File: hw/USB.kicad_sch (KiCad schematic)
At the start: 4 parts, among them J3 USB_C_Receptacle_USB2.0, U3 PUSB3FR4

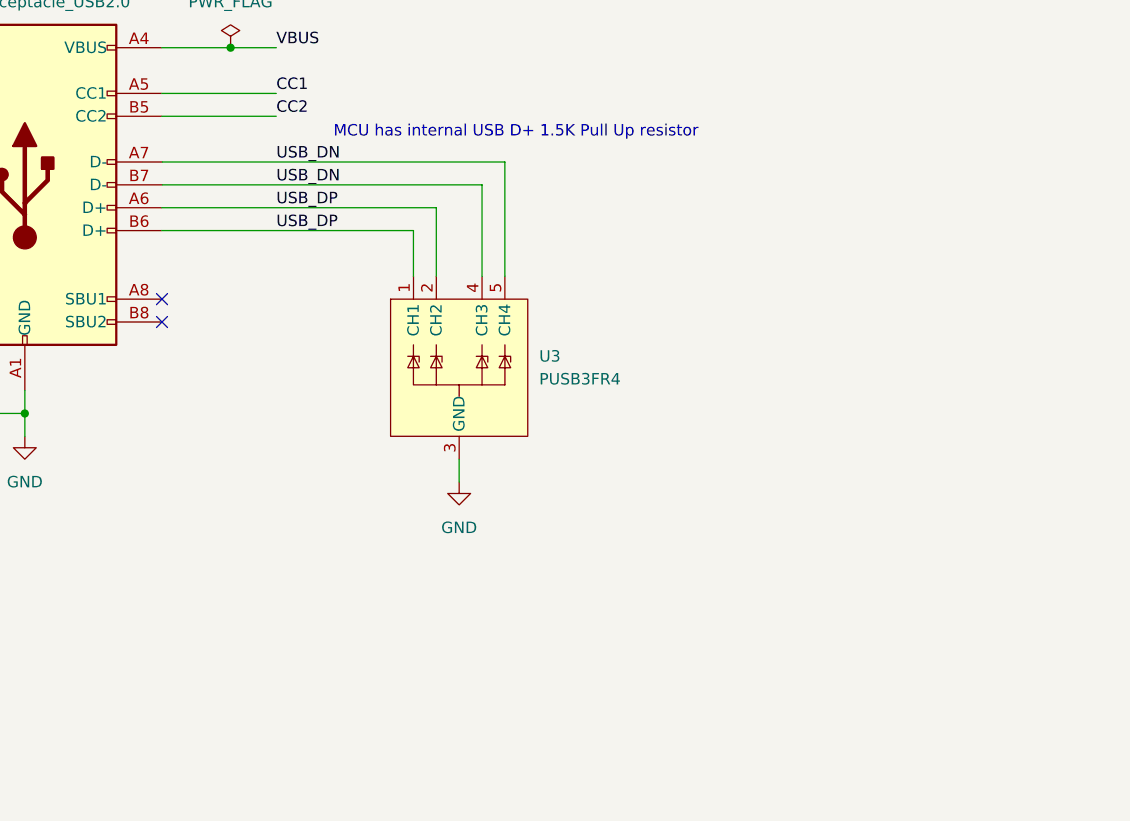
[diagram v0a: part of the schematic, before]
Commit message: routed USB
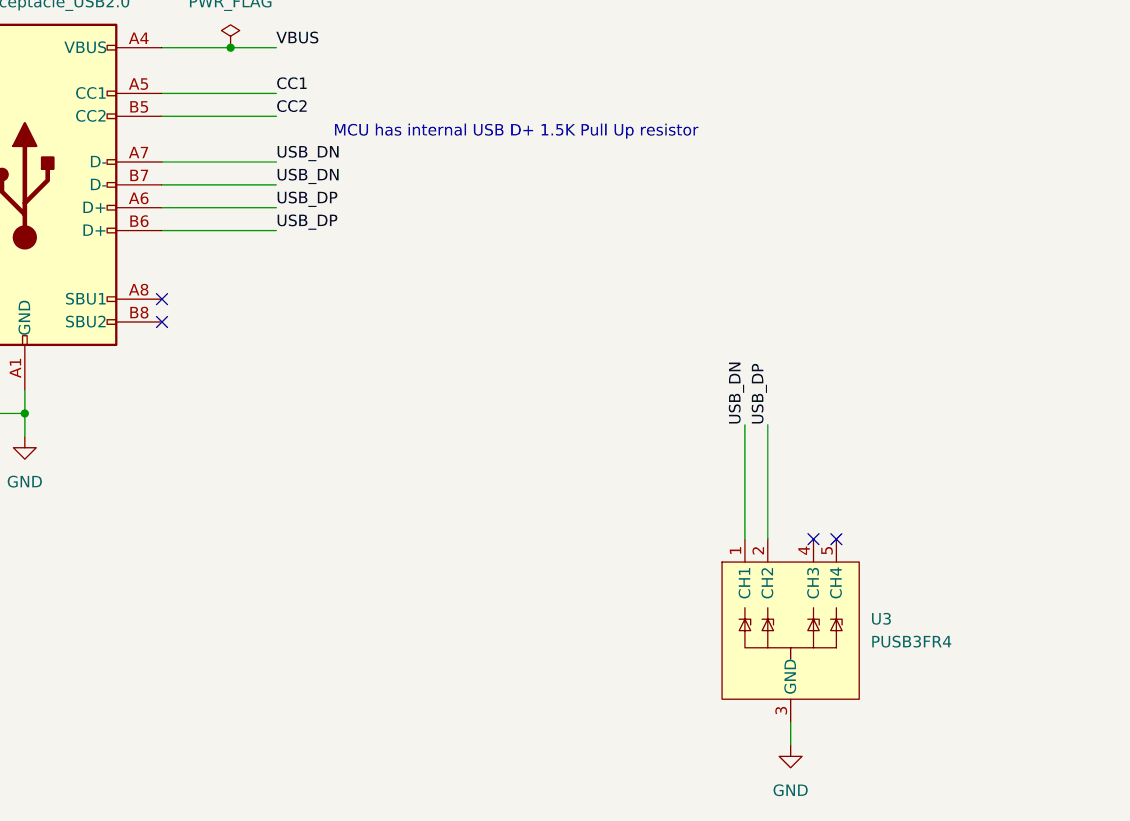
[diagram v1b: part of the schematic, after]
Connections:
- net USB_DN: now also U3.1 (CH1); no longer U3.4 (CH3), U3.5 (CH4)
- net USB_DP: no longer U3.1 (CH1)
- no-connect marks 2 -> 4
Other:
- moved on the sheet: U3
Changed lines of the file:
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@@
   (junction (at 48.26 106.68) (diameter 0) (color 0 0 0 0)
   )
+  (no_connect (at 138.43 120.65))
   (no_connect (at 63.5 93.98))
+  (no_connect (at 135.89 120.65))
   (no_connect (at 63.5 96.52))
   (wire (pts (xy 193.04 73.66) (xy 180.34 73.66))
@@
     (stroke (width 0) (type default))
   )
-  (wire (pts (xy 63.5 83.82) (xy 93.98 83.82))
+  (wire (pts (xy 63.5 83.82) (xy 76.2 83.82))
     (stroke (width 0) (type default))
   )
@@
     (stroke (width 0) (type default))
   )
-  (wire (pts (xy 63.5 81.28) (xy 99.06 81.28))
-    (stroke (width 0) (type default))
-  )
-  (wire (pts (xy 63.5 78.74) (xy 101.6 78.74))
-    (stroke (width 0) (type default))
-  )
-  (wire (pts (xy 101.6 91.44) (xy 101.6 78.74))
+  (wire (pts (xy 63.5 81.28) (xy 76.2 81.28))
+    (stroke (width 0) (type default))
+  )
+  (wire (pts (xy 63.5 78.74) (xy 76.2 78.74))
     (stroke (width 0) (type default))
   )
@@
     (stroke (width 0) (type default))
   )
-  (wire (pts (xy 91.44 91.44) (xy 91.44 86.36))
-    (stroke (width 0) (type default))
-  )
   (wire (pts (xy 71.12 66.04) (xy 76.2 66.04))
     (stroke (width 0) (type default))
   )
-  (wire (pts (xy 96.52 111.76) (xy 96.52 114.3))
-    (stroke (width 0) (type default))
-  )
-  (wire (pts (xy 99.06 91.44) (xy 99.06 81.28))
+  (wire (pts (xy 133.35 140.97) (xy 133.35 143.51))
+    (stroke (width 0) (type default))
+  )
+  (wire (pts (xy 130.81 120.65) (xy 130.81 107.95))
     (stroke (width 0) (type default))
   )
@@
     (stroke (width 0) (type default))
   )
-  (wire (pts (xy 63.5 86.36) (xy 91.44 86.36))
+  (wire (pts (xy 63.5 86.36) (xy 76.2 86.36))
     (stroke (width 0) (type default))
   )
@@
     (stroke (width 0) (type default))
   )
-  (wire (pts (xy 93.98 91.44) (xy 93.98 83.82))
+  (wire (pts (xy 128.27 120.65) (xy 128.27 107.95))
     (stroke (width 0) (type default))
   )
@@
   )
   (label "USB_DN" (at 76.2 78.74 0) (fields_autoplaced)
+    (effects (font (size 1.27 1.27)) (justify left bottom))
+  )
+  (label "USB_DN" (at 128.27 107.95 90) (fields_autoplaced)
     (effects (font (size 1.27 1.27)) (justify left bottom))
   )
@@
   (label "CC2" (at 180.34 86.36 180) (fields_autoplaced)
     (effects (font (size 1.27 1.27)) (justify right bottom))
+  )
+  (label "USB_DP" (at 130.81 107.95 90) (fields_autoplaced)
+    (effects (font (size 1.27 1.27)) (justify left bottom))
   )
   (label "CC1" (at 180.34 73.66 180) (fields_autoplaced)
@@
     )
   )
-  (symbol (lib_id "IotPi_Power_Protections:PUSB3FR4") (at 96.52 101.6 0) (unit 1)
-    (in_bom yes) (on_board yes) (dnp no) (fields_autoplaced)
-    (property "Reference" "U3" (at 105.41 100.33 0)
+  (symbol (lib_id "IotPi_Power_Protections:PUSB3FR4") (at 133.35 130.81 0) (unit 1)
+    (in_bom yes) (on_board yes) (dnp no) (fields_autoplaced)
+    (property "Reference" "U3" (at 142.24 129.54 0)
       (effects (font (size 1.27 1.27)) (justify left))
     )
-    (property "Value" "PUSB3FR4" (at 105.41 102.87 0)
+    (property "Value" "PUSB3FR4" (at 142.24 132.08 0)
       (effects (font (size 1.27 1.27)) (justify left))
     )
-    (property "Footprint" "IotPi_Package_DFN_QFN:Nexperia_DFN2510A-10" (at 96.52 101.6 0)
-      (effects (font (size 1.27 1.27)) hide)
-    )
-    (property "Datasheet" "" (at 96.52 101.6 0)
-      (effects (font (size 1.27 1.27)) hide)
-    )
-    (property "Description" "单向通道数: 4 反向截止电压(Vrwm): 3.3V@Max 击穿电压: 5.5V 峰值脉冲电流(Ipp)@10/1000us: - 最大钳位电压:" (at 96.52 101.6 0)
-      (effects (font (size 1.27 1.27)) hide)
-    )
-    (property "LCSC" "C503418" (at 96.52 101.6 0)
-      (effects (font (size 1.27 1.27)) hide)
-    )
-    (property "Vendor" "Nexperia(安世)" (at 96.52 101.6 0)
-      (effects (font (size 1.27 1.27)) hide)
-    )
-    (property "Vendor Model" "PUSB3FR4Z" (at 96.52 101.6 0)
+    (property "Footprint" "IotPi_Package_DFN_QFN:Nexperia_DFN2510A-10" (at 133.35 130.81 0)
+      (effects (font (size 1.27 1.27)) hide)
+    )
+    (property "Datasheet" "" (at 133.35 130.81 0)
+      (effects (font (size 1.27 1.27)) hide)
+    )
+    (property "Description" "单向通道数: 4 反向截止电压(Vrwm): 3.3V@Max 击穿电压: 5.5V 峰值脉冲电流(Ipp)@10/1000us: - 最大钳位电压:" (at 133.35 130.81 0)
+      (effects (font (size 1.27 1.27)) hide)
+    )
+    (property "LCSC" "C503418" (at 133.35 130.81 0)
+      (effects (font (size 1.27 1.27)) hide)
+    )
+    (property "Vendor" "Nexperia(安世)" (at 133.35 130.81 0)
+      (effects (font (size 1.27 1.27)) hide)
+    )
+    (property "Vendor Model" "PUSB3FR4Z" (at 133.35 130.81 0)
       (effects (font (size 1.27 1.27)) hide)
     )
@@
     )
   )
-  (symbol (lib_id "power:GND") (at 96.52 114.3 0) (unit 1)
-    (in_bom yes) (on_board yes) (dnp no) (fields_autoplaced)
-    (property "Reference" "#PWR07" (at 96.52 120.65 0)
-      (effects (font (size 1.27 1.27)) hide)
-    )
-    (property "Value" "GND" (at 96.52 119.38 0)
-      (effects (font (size 1.27 1.27)))
-    )
-    (property "Footprint" "" (at 96.52 114.3 0)
-      (effects (font (size 1.27 1.27)) hide)
-    )
-    (property "Datasheet" "" (at 96.52 114.3 0)
-      (effects (font (size 1.27 1.27)) hide)
-    )
+  (symbol (lib_id "power:GND") (at 133.35 143.51 0) (unit 1)
+    (in_bom yes) (on_board yes) (dnp no) (fields_autoplaced)
+    (property "Reference" "#PWR07" (at 133.35 149.86 0)
+      (effects (font (size 1.27 1.27)) hide)
+    )
+    (property "Value" "GND" (at 133.35 148.59 0)
+      (effects (font (size 1.27 1.27)))
+    )
+    (property "Footprint" "" (at 133.35 143.51 0)
+      (effects (font (size 1.27 1.27)) hide)
+    )
+    (property "Datasheet" "" (at 133.35 143.51 0)
+      (effects (font (size 1.27 1.27)) hide)
+    )
